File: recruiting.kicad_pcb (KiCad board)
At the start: 2 copper layers, 1 part

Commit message: fatti alcuni calcoli secondo datasheet per il dimensionamento delle resistenze Rfb1/2 e dimensionamento del MOSFET a canale P per lo switch
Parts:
- removed C1: 1F, Capacitor_SMD:C_0805_2012Metric
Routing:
- net Net-(C1-Pad1): track 57.5 -> 0.00 mm
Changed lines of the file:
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@@
   )
   (net 0 "")
-  (net 1 "Net-(C1-Pad1)")
-  (footprint "Capacitor_SMD:C_0805_2012Metric" (layer "F.Cu")
-    (at 150.75 88.75)
-    (descr "Capacitor SMD 0805 (2012 Metric), square (rectangular) end terminal, IPC_7351 nominal, (Body size source: IPC-SM-782 page 76, https://www.pcb-3d.com/wordpress/wp-content/uploads/ipc-sm-782a_amendment_1_and_2.pdf, https://docs.google.com/spreadsheets/d/1BsfQQcO9C6DZCsRaXUlFlo91Tg2WpOkGARC1WS5S8t0/edit?usp=sharing), generated with kicad-footprint-generator")
-    (tags "capacitor")
-    (property "Sheetfile" "template.kicad_sch")
-    (property "Sheetname" "")
-    (attr smd)
-    (fp_text reference "C1" (at 0 -1.68) (layer "F.SilkS")
-      (effects (font (size 1 1) (thickness 0.15)))
-    )
-    (fp_text value "1F" (at 0 1.68) (layer "F.Fab")
-      (effects (font (size 1 1) (thickness 0.15)))
-    )
-    (fp_text user "${REFERENCE}" (at 0 0) (layer "F.Fab")
-      (effects (font (size 0.5 0.5) (thickness 0.08)))
-    )
-    (fp_line (start -0.261252 -0.735) (end 0.261252 -0.735) (layer "F.SilkS") (width 0.12))
-    (fp_line (start -0.261252 0.735) (end 0.261252 0.735) (layer "F.SilkS") (width 0.12))
-    (fp_line (start 1.7 0.98) (end -1.7 0.98) (layer "F.CrtYd") (width 0.05))
-    (fp_line (start 1.7 -0.98) (end 1.7 0.98) (layer "F.CrtYd") (width 0.05))
-    (fp_line (start -1.7 0.98) (end -1.7 -0.98) (layer "F.CrtYd") (width 0.05))
-    (fp_line (start -1.7 -0.98) (end 1.7 -0.98) (layer "F.CrtYd") (width 0.05))
-    (fp_line (start 1 0.625) (end -1 0.625) (layer "F.Fab") (width 0.1))
-    (fp_line (start 1 -0.625) (end 1 0.625) (layer "F.Fab") (width 0.1))
-    (fp_line (start -1 0.625) (end -1 -0.625) (layer "F.Fab") (width 0.1))
-    (fp_line (start -1 -0.625) (end 1 -0.625) (layer "F.Fab") (width 0.1))
-    (pad "1" smd roundrect (at -0.95 0) (size 1 1.45) (layers "F.Cu" "F.Paste" "F.Mask") (roundrect_rratio 0.25)
-      (net 1 "Net-(C1-Pad1)") (pintype "passive"))
-    (pad "2" smd roundrect (at 0.95 0) (size 1 1.45) (layers "F.Cu" "F.Paste" "F.Mask") (roundrect_rratio 0.25)
-      (net 1 "Net-(C1-Pad1)") (pintype "passive"))
-    (model "${KICAD6_3DMODEL_DIR}/Capacitor_SMD.3dshapes/C_0805_2012Metric.wrl"
-      (offset (xyz 0 0 0))
-      (scale (xyz 1 1 1))
-      (rotate (xyz 0 0 0))
-    )
-  )
-  (segment (start 143 86.75) (end 146.5 83.25) (width 0.25) (layer "F.Cu") (net 1))
-  (segment (start 146.5 83.25) (end 147.25 83.25) (width 0.25) (layer "F.Cu") (net 1))
-  (segment (start 156.25 83.25) (end 159.375 86.375) (width 0.25) (layer "F.Cu") (net 1))
-  (segment (start 151.15 83.95) (end 151.15 83.25) (width 0.25) (layer "F.Cu") (net 1))
-  (segment (start 148.75 83.95) (end 148.75 83.25) (width 0.25) (layer "F.Cu") (net 1))
-  (segment (start 145 88.75) (end 143 86.75) (width 0.25) (layer "F.Cu") (net 1))
-  (segment (start 149.8 88.75) (end 145 88.75) (width 0.25) (layer "F.Cu") (net 1))
-  (segment (start 150.55 83.25) (end 150.55 83.95) (width 0.25) (layer "F.Cu") (net 1))
-  (segment (start 159.375 86.375) (end 157 88.75) (width 0.25) (layer "F.Cu") (net 1))
-  (segment (start 154.15 82.55) (end 154.15 83.25) (width 0.25) (layer "F.Cu") (net 1))
-  (segment (start 155.35 82.55) (end 155.35 82.95) (width 0.25) (layer "F.Cu") (net 1))
-  (segment (start 148.75 83.25) (end 148.75 82.55) (width 0.25) (layer "F.Cu") (net 1))
-  (segment (start 149.95 83.95) (end 149.95 83.25) (width 0.25) (layer "F.Cu") (net 1))
-  (segment (start 149.35 82.55) (end 149.35 83.25) (width 0.25) (layer "F.Cu") (net 1))
-  (segment (start 151.75 82.55) (end 151.75 83.25) (width 0.25) (layer "F.Cu") (net 1))
-  (segment (start 152.95 83.25) (end 152.95 83.95) (width 0.25) (layer "F.Cu") (net 1))
-  (segment (start 150.55 82.55) (end 150.55 83.25) (width 0.25) (layer "F.Cu") (net 1))
-  (segment (start 148.15 82.55) (end 148.15 82.95) (width 0.25) (layer "F.Cu") (net 1))
-  (segment (start 153.55 83.25) (end 153.55 82.55) (width 0.25) (layer "F.Cu") (net 1))
-  (segment (start 154.75 83.95) (end 154.75 83.25) (width 0.25) (layer "F.Cu") (net 1))
-  (segment (start 152.95 82.55) (end 152.95 83.25) (width 0.25) (layer "F.Cu") (net 1))
-  (segment (start 155.65 83.25) (end 156.25 83.25) (width 0.25) (layer "F.Cu") (net 1))
-  (segment (start 148.15 82.95) (end 148.15 83.95) (width 0.25) (layer "F.Cu") (net 1))
-  (segment (start 151.15 83.25) (end 151.15 82.55) (width 0.25) (layer "F.Cu") (net 1))
-  (segment (start 149.95 83.25) (end 149.95 82.55) (width 0.25) (layer "F.Cu") (net 1))
-  (segment (start 147.55 82.95) (end 147.55 82.55) (width 0.25) (layer "F.Cu") (net 1))
-  (segment (start 152.35 83.25) (end 152.35 82.55) (width 0.25) (layer "F.Cu") (net 1))
-  (segment (start 149.35 83.25) (end 149.35 83.95) (width 0.25) (layer "F.Cu") (net 1))
-  (segment (start 154.75 83.25) (end 154.75 82.55) (width 0.25) (layer "F.Cu") (net 1))
-  (segment (start 153.55 83.95) (end 153.55 83.25) (width 0.25) (layer "F.Cu") (net 1))
-  (segment (start 154.15 83.25) (end 154.15 83.95) (width 0.25) (layer "F.Cu") (net 1))
-  (segment (start 157 88.75) (end 151.7 88.75) (width 0.25) (layer "F.Cu") (net 1))
-  (segment (start 152.35 83.95) (end 152.35 83.25) (width 0.25) (layer "F.Cu") (net 1))
-  (segment (start 151.75 83.25) (end 151.75 83.95) (width 0.25) (layer "F.Cu") (net 1))
-  (arc (start 150.55 83.95) (mid 150.637868 84.162132) (end 150.85 84.25) (width 0.25) (layer "F.Cu") (net 1))
-  (arc (start 153.85 82.25) (mid 154.062132 82.337868) (end 154.15 82.55) (width 0.25) (layer "F.Cu") (net 1))
-  (arc (start 152.35 82.55) (mid 152.437868 82.337868) (end 152.65 82.25) (width 0.25) (layer "F.Cu") (net 1))
-  (arc (start 149.95 82.55) (mid 150.037868 82.337868) (end 150.25 82.25) (width 0.25) (layer "F.Cu") (net 1))
-  (arc (start 152.65 82.25) (mid 152.862132 82.337868) (end 152.95 82.55) (width 0.25) (layer "F.Cu") (net 1))
-  (arc (start 148.45 84.25) (mid 148.662132 84.162132) (end 148.75 83.95) (width 0.25) (layer "F.Cu") (net 1))
-  (arc (start 154.75 82.55) (mid 154.837868 82.337868) (end 155.05 82.25) (width 0.25) (layer "F.Cu") (net 1))
-  (arc (start 151.45 82.25) (mid 151.662132 82.337868) (end 151.75 82.55) (width 0.25) (layer "F.Cu") (net 1))
-  (arc (start 151.15 82.55) (mid 151.237868 82.337868) (end 151.45 82.25) (width 0.25) (layer "F.Cu") (net 1))
-  (arc (start 154.15 83.95) (mid 154.237868 84.162132) (end 154.45 84.25) (width 0.25) (layer "F.Cu") (net 1))
-  (arc (start 148.75 82.55) (mid 148.837868 82.337868) (end 149.05 82.25) (width 0.25) (layer "F.Cu") (net 1))
-  (arc (start 147.55 82.55) (mid 147.637868 82.337868) (end 147.85 82.25) (width 0.25) (layer "F.Cu") (net 1))
-  (arc (start 147.85 82.25) (mid 148.062132 82.337868) (end 148.15 82.55) (width 0.25) (layer "F.Cu") (net 1))
-  (arc (start 150.25 82.25) (mid 150.462132 82.337868) (end 150.55 82.55) (width 0.25) (layer "F.Cu") (net 1))
-  (arc (start 152.95 83.95) (mid 153.037868 84.162132) (end 153.25 84.25) (width 0.25) (layer "F.Cu") (net 1))
-  (arc (start 155.35 82.95) (mid 155.437868 83.162132) (end 155.65 83.25) (width 0.25) (layer "F.Cu") (net 1))
-  (arc (start 153.55 82.55) (mid 153.637868 82.337868) (end 153.85 82.25) (width 0.25) (layer "F.Cu") (net 1))
-  (arc (start 149.65 84.25) (mid 149.862132 84.162132) (end 149.95 83.95) (width 0.25) (layer "F.Cu") (net 1))
-  (arc (start 151.75 83.95) (mid 151.837868 84.162132) (end 152.05 84.25) (width 0.25) (layer "F.Cu") (net 1))
-  (arc (start 150.85 84.25) (mid 151.062132 84.162132) (end 151.15 83.95) (width 0.25) (layer "F.Cu") (net 1))
-  (arc (start 153.25 84.25) (mid 153.462132 84.162132) (end 153.55 83.95) (width 0.25) (layer "F.Cu") (net 1))
-  (arc (start 149.35 83.95) (mid 149.437868 84.162132) (end 149.65 84.25) (width 0.25) (layer "F.Cu") (net 1))
-  (arc (start 148.15 83.95) (mid 148.237868 84.162132) (end 148.45 84.25) (width 0.25) (layer "F.Cu") (net 1))
-  (arc (start 147.25 83.25) (mid 147.462132 83.162132) (end 147.55 82.95) (width 0.25) (layer "F.Cu") (net 1))
-  (arc (start 152.05 84.25) (mid 152.262132 84.162132) (end 152.35 83.95) (width 0.25) (layer "F.Cu") (net 1))
-  (arc (start 154.45 84.25) (mid 154.662132 84.162132) (end 154.75 83.95) (width 0.25) (layer "F.Cu") (net 1))
-  (arc (start 155.05 82.25) (mid 155.262132 82.337868) (end 155.35 82.55) (width 0.25) (layer "F.Cu") (net 1))
-  (arc (start 149.05 82.25) (mid 149.262132 82.337868) (end 149.35 82.55) (width 0.25) (layer "F.Cu") (net 1))
 )

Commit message: alcune modifiche ai package di alcuni componenti e continuazione del design del circuito stampato
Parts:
- added 3V: JST_NV_B02P-NV_1x02_P5.00mm_Vertical, Connector_JST:JST_NV_B02P-NV_1x02_P5.00mm_Vertical, F.Cu at (161.2, 102.4)
- added 5V: JST_NV_B02P-NV_1x02_P5.00mm_Vertical, Connector_JST:JST_NV_B02P-NV_1x02_P5.00mm_Vertical, F.Cu at (161.1, 83.3)
- added C1: 10nF, Capacitor_SMD:C_0603_1608Metric, F.Cu at (108.8, 89.6)
- added C2: 1uF, Capacitor_SMD:C_0603_1608Metric, F.Cu at (114.4, 82.9)
- added Cadj'1: 1 nF, Capacitor_SMD:C_0402_1005Metric, F.Cu at (135.7, 106.4)
- added Cadj1: 1 nF, Capacitor_SMD:C_0402_1005Metric, F.Cu at (137.5, 96.0)
- added Cbyp'1: 1,8 uF, Capacitor_SMD:C_0603_1608Metric, F.Cu at (142.6, 100.1)
- added Cbyp1: 3,3 uF, Capacitor_SMD:C_0603_1608Metric, F.Cu at (142.5, 96.0)
- added Cff'1: 0,39 uF, Capacitor_SMD:C_0603_1608Metric, F.Cu at (148.2, 101.2)
- added Cff1: 1,8 uF, Capacitor_SMD:C_0603_1608Metric, F.Cu at (150.4, 84.2)
- added Cin'1: 3,3uF, Capacitor_SMD:C_0603_1608Metric, F.Cu at (140.8, 100.1)
- added Cin1: 39uF, Capacitor_SMD:C_0603_1608Metric, F.Cu at (140.8, 96.0)
- added Cout'1: 150 nF, Capacitor_SMD:C_1206_3216Metric, F.Cu at (153.2, 105.7)
- added Cout1: 68 nF, Capacitor_SMD:C_1206_3216Metric, F.Cu at (154.1, 88.3)
- added Creg1: 0,1 uF, Capacitor_SMD:C_01005_0402Metric, F.Cu at (118.2, 112.7)
- added Cvcc1: 0,47 uF, Capacitor_SMD:C_0402_1005Metric, F.Cu at (132.7, 93.4)
- added Cvcc2: 0,47 uF, Capacitor_SMD:C_0402_1005Metric, F.Cu at (133.0, 104.6)
- added D1: PMEG040V050EPD, Package_TO_SOT_SMD:Nexperia_CFP15_SOT-1289, F.Cu at (127.0, 84.2)
- added D2: PMEG040V050EPD, Package_TO_SOT_SMD:Nexperia_CFP15_SOT-1289, F.Cu at (126.0, 117.1)
- added Dl1: LED, Diode_SMD:D_0805_2012Metric, F.Cu at (106.4, 87.0)
- added Dz1: BZV55B7V5, Diode_SMD:D_MiniMELF, F.Cu at (110.8, 104.5)
- added Dz2: BZV55B2V4, Diode_SMD:D_MiniMELF, F.Cu at (104.7, 101.5)
- added L'1: 330 uH, Inductor_SMD:L_Wuerth_HCI-2212, F.Cu at (142.2, 119.8)
- added L1: 56 uH, Inductor_SMD:L_Pulse_PA4344, F.Cu at (139.2, 79.6)
- added Q1: IRF9383M, Package_DirectFET:DirectFET_MX, F.Cu at (125.7, 92.9)
- added Q2: IRF9383M, Package_DirectFET:DirectFET_MX, F.Cu at (125.7, 108.2)
- added R1: 560, Resistor_SMD:R_0603_1608Metric, F.Cu at (107.8, 101.7)
- added R2: 560Ω, Resistor_SMD:R_0603_1608Metric, F.Cu at (107.8, 99.7)
- added R3: 560Ω, Resistor_SMD:R_0603_1608Metric, F.Cu at (111.8, 101.7)
- added R4: 180 mΩ, Resistor_SMD:R_0805_2012Metric, F.Cu at (154.1, 84.2)
- added R4'1: 1,2 Ω, Resistor_SMD:R_0805_2012Metric, F.Cu at (153.2, 101.2)
- added R5: 100Ω, Resistor_SMD:R_0603_1608Metric, F.Cu at (108.8, 93.3)
- added RT1: 47KΩ, Resistor_SMD:R_0402_1005Metric, F.Cu at (139.7, 106.4)
- added RT1'1: 3,3KΩ, Resistor_SMD:R_0402_1005Metric, F.Cu at (141.4, 104.7)
- added RT2: 82KΩ, Resistor_SMD:R_0603_1608Metric, F.Cu at (135.2, 95.4)
- added Radj'1: 180Ω, Resistor_SMD:R_0402_1005Metric, F.Cu at (137.7, 106.9)
- added Radj1: 1 KΩ, Resistor_SMD:R_0603_1608Metric, F.Cu at (139.0, 96.0)
- added Rfb1: 3,3KΩ, Resistor_SMD:R_0603_1608Metric, F.Cu at (152.2, 84.2)
- added Rfb1'1: 12KΩ, Resistor_SMD:R_0603_1608Metric, F.Cu at (150.6, 101.2)
- added Rfb2: 10KΩ, Resistor_SMD:R_0603_1608Metric, F.Cu at (150.4, 87.3)
- added Rfb2'1: 18KΩ, Resistor_SMD:R_0603_1608Metric, F.Cu at (150.6, 105.1)
- added Rin1: 10Ω, Resistor_SMD:R_0402_1005Metric, F.Cu at (114.2, 110.1)
- added Rl1: 330Ω, Resistor_SMD:R_0402_1005Metric, F.Cu at (108.8, 86.6)
- added Rl2: 120KΩ, Resistor_SMD:R_0402_1005Metric, F.Cu at (111.5, 82.8)
- added Rout1: 10KΩ, Resistor_SMD:R_0603_1608Metric, F.Cu at (108.8, 96.7)
- added Rsen1: 10mΩ, Resistor_SMD:R_0805_2012Metric, F.Cu at (129.6, 98.1)
- added Rsen2: 10mΩ, Resistor_SMD:R_0805_2012Metric, F.Cu at (129.6, 102.5)
- added Rsh1: 1mΩ, Resistor_SMD:R_0805_2012Metric, F.Cu at (120.0, 111.5)
- added U1: LM25085MM, Package_SO:MSOP-8_3x3mm_P0.65mm, F.Cu at (136.9, 92.6)
- added U2: LM25085MM, Package_SO:MSOP-8_3x3mm_P0.65mm, F.Cu at (137.3, 103.8)
- added U3: LM358, Package_SO:SOIC-8_3.9x4.9mm_P1.27mm, F.Cu at (113.0, 96.3)
- added UL1: NE555D, Package_SO:SOIC-8_3.9x4.9mm_P1.27mm, F.Cu at (113.1, 87.9)
- added Us1: LTC6102xMS8, Package_SO:MSOP-8_3x3mm_P0.65mm, F.Cu at (114.2, 112.7)
- added Vin: JST_NV_B02P-NV_1x02_P5.00mm_Vertical, Connector_JST:JST_NV_B02P-NV_1x02_P5.00mm_Vertical, F.Cu at (111.5, 121.4)
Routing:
- net Net-(D1-Pad3): track 0.00 -> 31.6 mm
- net /Buck controller/Vin_B: track 0.00 -> 30.8 mm
- net FB_1: track 0.00 -> 21.8 mm
- net ISEN_1: track 0.00 -> 20.6 mm
- net FB_2: track 0.00 -> 14.1 mm
- net Net-(D2-Pad3): track 0.00 -> 13.3 mm
- net GATE_2: track 0.00 -> 12.6 mm
- net GATE_1: track 0.00 -> 9.76 mm
- net GND: track 0.00 -> 8.71 mm
- net Vin: track 0.00 -> 4.54 mm
- net Net-(RT2-Pad2): track 0.00 -> 4.27 mm
- net Net-(Cadj'1-Pad1): track 0.00 -> 3.92 mm
- net Net-(Cadj1-Pad1): track 0.00 -> 3.48 mm
- net Net-(Cvcc2-Pad2): track 0.00 -> 2.16 mm
- net Net-(Cvcc1-Pad2): track 0.00 -> 2.12 mm
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- added copper zone on F.Cu, net (none)
- added copper zone on F.Cu, net 5V3A

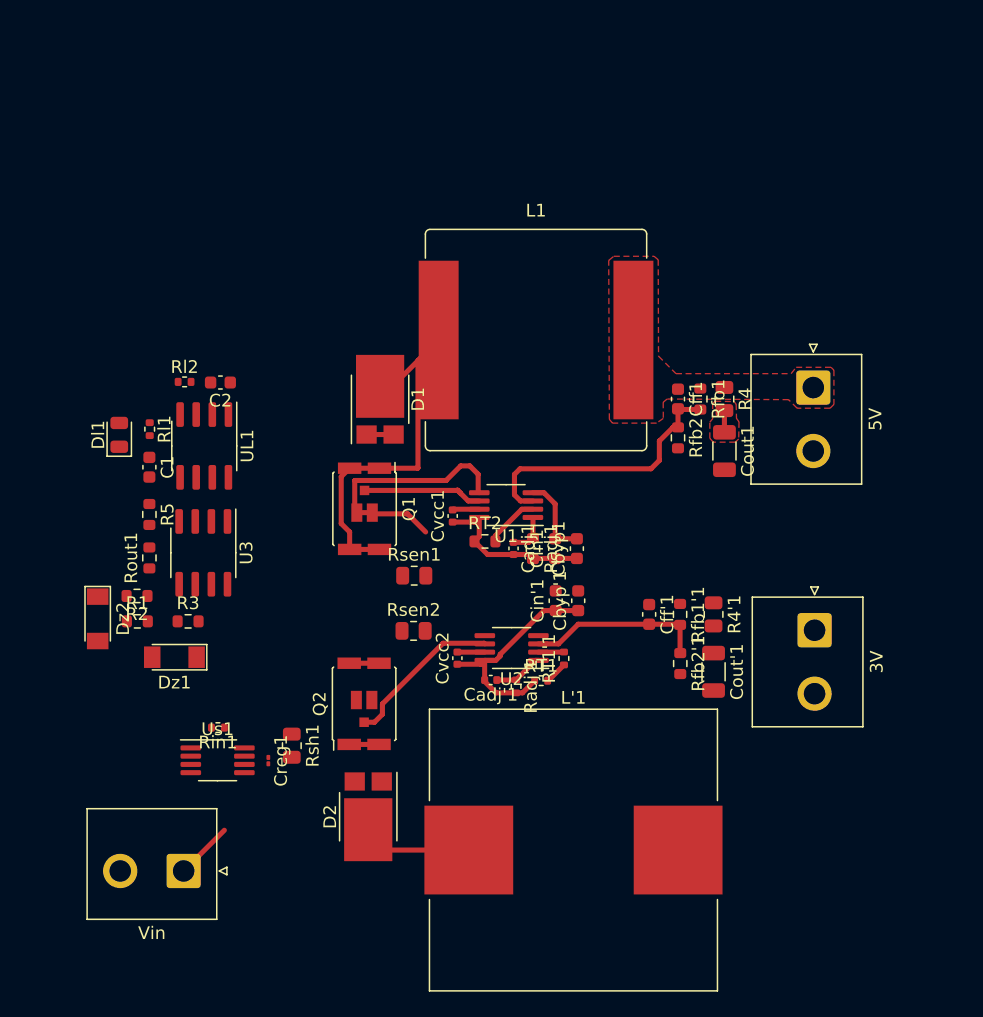
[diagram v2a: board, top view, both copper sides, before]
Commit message: completato il file pcb, creato un file gerber nella directory 'output' e creato i file pdf dello schema nella directory 'docs'
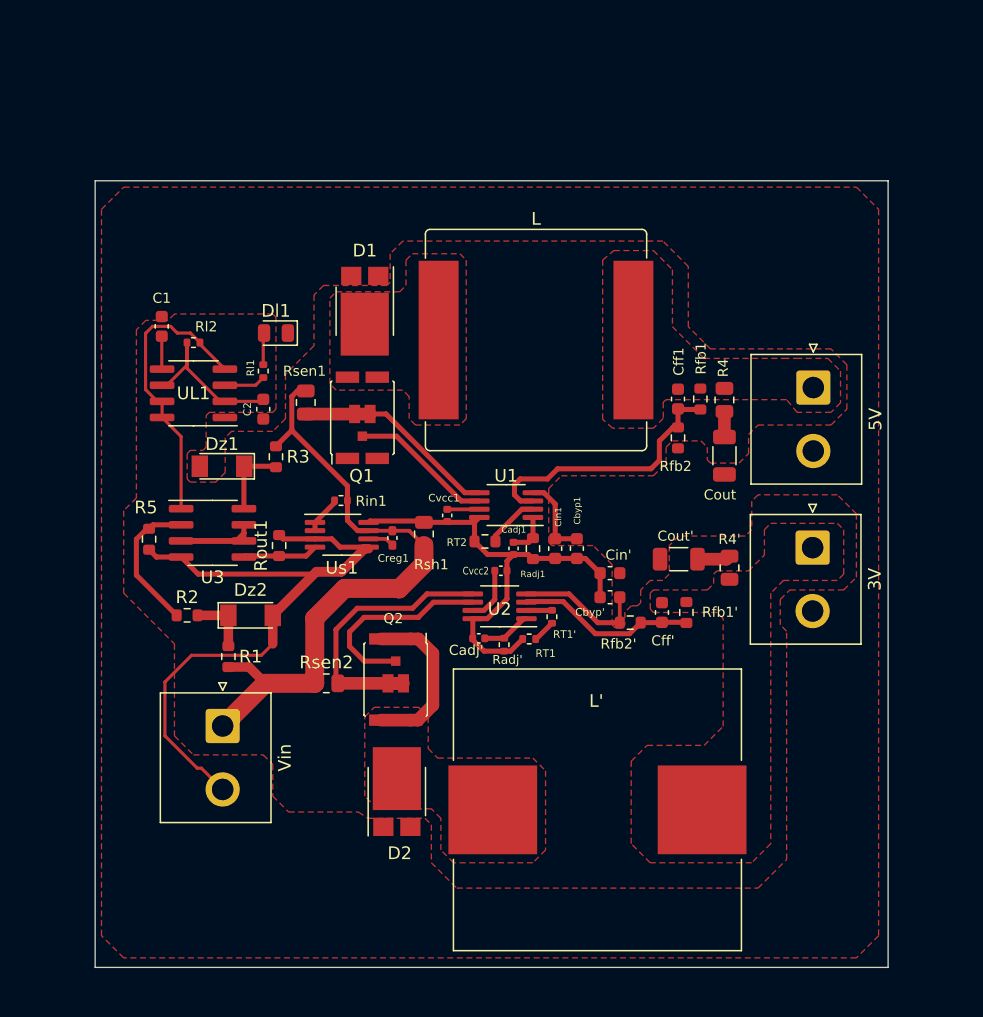
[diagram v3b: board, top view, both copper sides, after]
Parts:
- Creg1: footprint Capacitor_SMD:C_01005_0402Metric -> Capacitor_SMD:C_0402_1005Metric_Pad0.74x0.62mm_HandSolder
- moved Rin1 20.4 mm to (123.9, 92.2)
- moved Us1 20.3 mm to (123.9, 94.9)
- moved Creg1 20.1 mm to (127.9, 95.2)
- moved Rsh1 19.7 mm to (130.4, 94.8), turned to 90 degrees
- moved Rsen1 16.1 mm to (121.1, 84.5), turned to -90 degrees
- moved Dz1 15.5 mm to (114.5, 89.5)
- moved Dl1 14.7 mm to (118.8, 79.0), turned to 180 degrees
- moved R3 14.7 mm to (118.8, 88.8), turned to -90 degrees
- moved Dz2 12.1 mm to (116.8, 101.2), turned to 0 degrees
- moved Vin 11.8 mm to (114.5, 110.0), turned to -90 degrees
- moved C1 11.1 mm to (109.8, 78.5)
- moved Rout1 10.3 mm to (119.0, 95.8)
- moved Rl1 10.1 mm to (117.8, 82.0)
- moved Cout' 9.29 mm to (150.5, 96.8), turned to 180 degrees
- moved Rsen2 8.03 mm to (122.7, 106.6)
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- renumbered Cadj'1 to Cadj', Cbyp'1 to Cbyp', Cff'1 to Cff', Cin'1 to Cin', Cout1 to Cout, Cout'1 to Cout', L1 to L, L'1 to L', R4'1 to R4', RT1'1 to RT1', Radj'1 to Radj', Rfb1'1 to Rfb1', Rfb2'1 to Rfb2'
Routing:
- net GND: track 8.71 -> 75.6 mm
- net Vin: track 4.54 -> 50.6 mm
- net Net-(D1-Pad3): track 31.6 -> 0.00 mm
- net /Shunt monitor/Vout: track 0.00 -> 23.1 mm
- net ISEN_2: track 0.00 -> 22.3 mm
- net Net-(C2-Pad2): track 0.00 -> 13.6 mm
- net Net-(U3-Pad3): track 0.00 -> 11.4 mm
- net Net-(R2-Pad1): track 0.00 -> 11.3 mm
- net /Buck controller/Vin_B: track 30.8 -> 36.8 mm
- net Net-(Rout1-Pad1): track 0.00 -> 5.93 mm
- net Net-(Dz1-Pad1): track 0.00 -> 5.89 mm
- net Net-(Dz2-Pad1): track 0.00 -> 4.85 mm
- net GATE_2: track 12.6 -> 15.9 mm
- net Net-(Rl1-Pad2): track 0.00 -> 3.28 mm
- net ISEN_1: track 20.6 -> 17.5 mm
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- added copper zone on F.Cu, net 3,3V0,5A
- added copper zone on F.Cu, net GND
- added copper zone on F.Cu, net Net-(D1-Pad3)
- added copper zone on F.Cu, net Net-(D2-Pad3)
- removed copper zone on F.Cu, net (none)
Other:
- board outline added: 62.5 x 62 mm
